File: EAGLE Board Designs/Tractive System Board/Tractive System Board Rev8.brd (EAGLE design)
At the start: 200 x 65 mm, 143 parts, among them J1 CONNECTOR-5_MICRO_V7S_, J2 CONNECTOR-5_MICRO_V6S_, J3 CONNECTOR-8_μF_T_V_BLACK, K1 RELAY_SPST_NO_D_24, Q2 TRANSISTOR_N_MOS__PMV15ENEA, U10 LTC6994-2, U5 RELAY_SOLIDSTATE_NO_AB38S-Q-A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, U6 LT8315, U7 AMC3330_AIRGAP, U8 AMC3330_AIRGAP

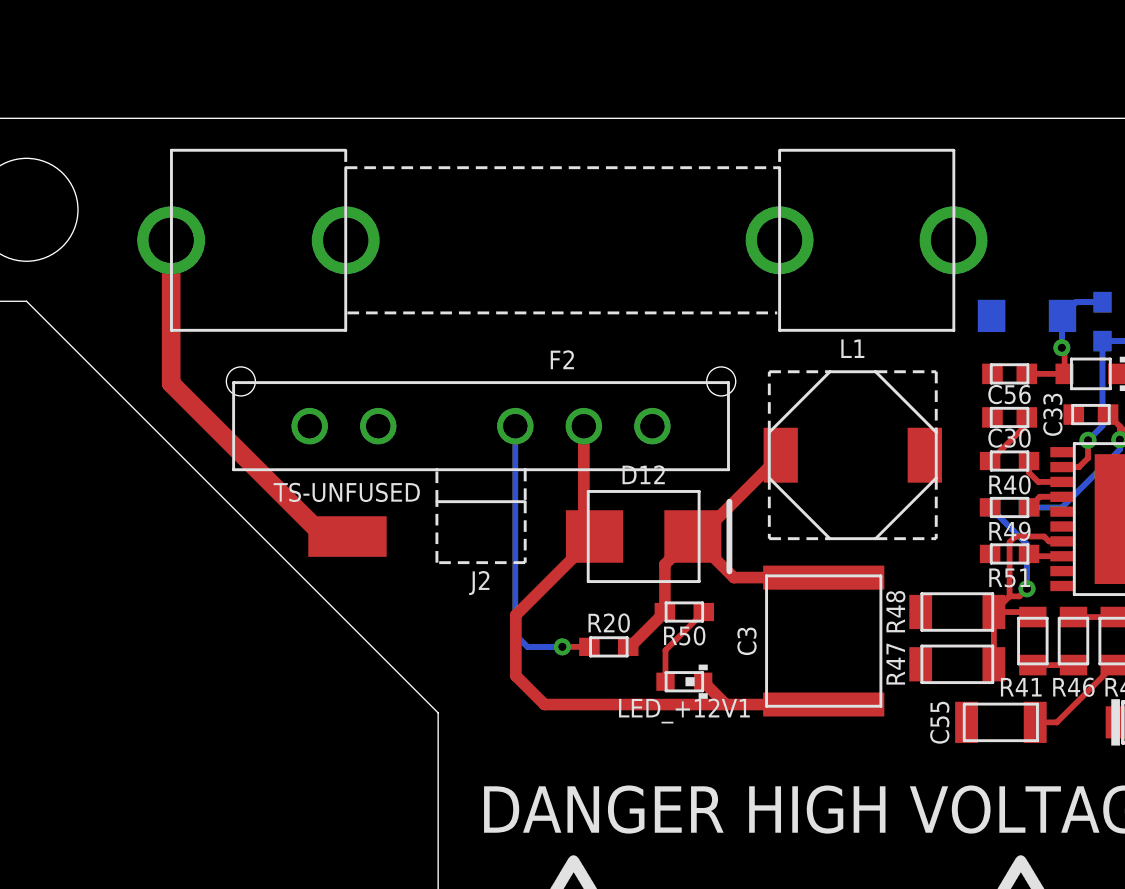
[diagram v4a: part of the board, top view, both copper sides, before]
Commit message: tsb-rev8-layout-update
space between connector and fuse on TS- side
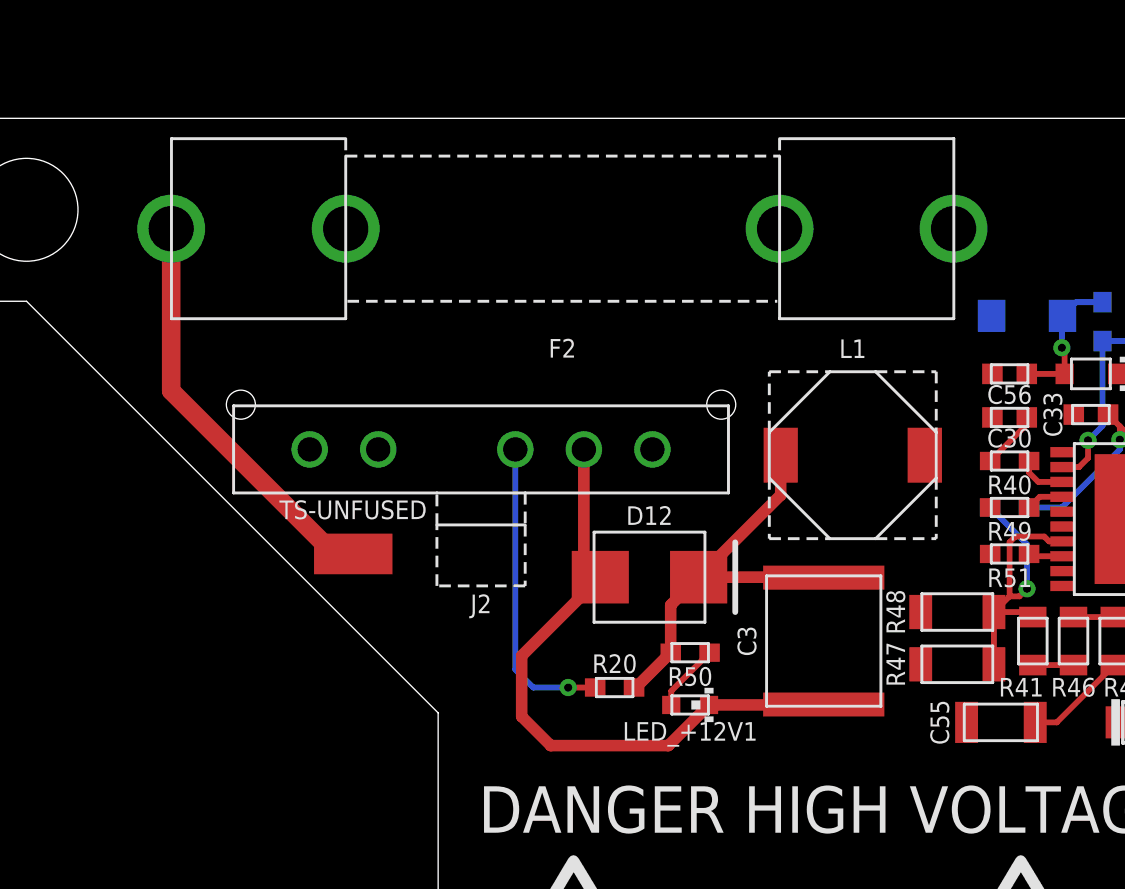
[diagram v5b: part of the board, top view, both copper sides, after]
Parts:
- moved R50 1.80 mm to (33.0, -23.4)
- moved D12 1.80 mm to (31.2, -20.1)
- moved R20 1.80 mm to (29.7, -24.9)
- moved LED_+12V1 1.05 mm to (33.0, -25.7)
- moved J2 1.02 mm to (23.9, -14.5)
- moved TS-UNFUSED 0.80 mm to (18.3, -19.1)
- moved F2 0.51 mm to (27.4, -4.83)
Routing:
- net TS-UNFUSED: track 34.4 -> 36.6 mm
- net TS-FUSED: track 91.0 -> 91.9 mm
- net AIL+: track 12.6 -> 13.4 mm
- net TS+12V: track 18.7 -> 19.5 mm
- net N$44: track 3.74 -> 2.98 mm

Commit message: tsb-rev8-layout-update
Made buck convert PGND connections to internal plane
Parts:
- moved D9 1.55 mm to (49.3, -8.89), flipped to the top, turned to 0 degrees
- moved R30 0.25 mm to (96.5, -47.0)
- moved R42 0.25 mm to (95.0, -47.0)
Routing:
- net PGND: track 1.31 -> 24.4 mm, vias 1 -> 11
- net TS+12V: track 19.5 -> 32.7 mm
- net IT+: track 95.8 -> 90.0 mm
- net DCDC_ENABLE: track 75.1 -> 70.7 mm
- net N$55: track 6.26 -> 7.71 mm
- net PRECHARGE_OK: track 82.3 -> 82.9 mm
- net GND: track 97.8 -> 98.5 mm

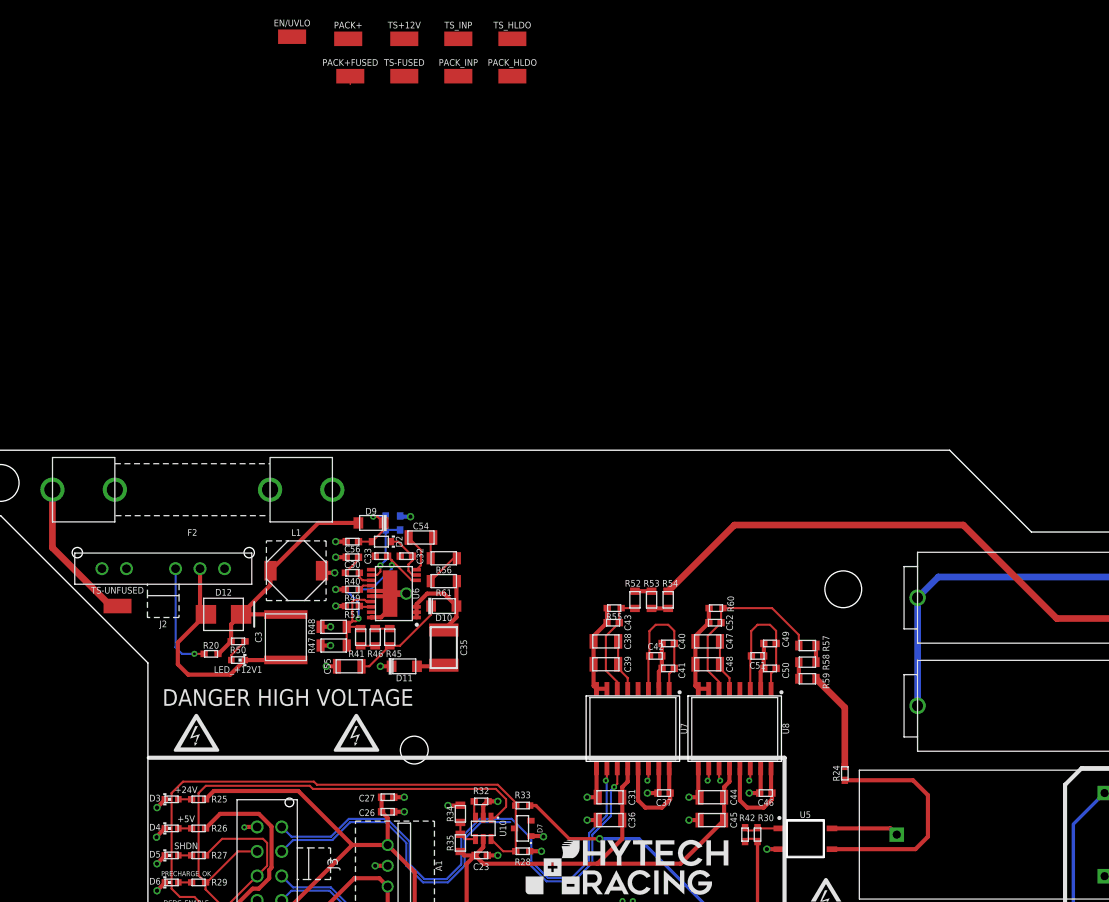
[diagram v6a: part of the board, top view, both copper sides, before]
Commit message: tsb-rev8-layout-update
Finished buck converter routing. Routed TS-FUSED to iso amps and buck. Placed TPs. Readjusted all via drill sizes to match hv pcb width
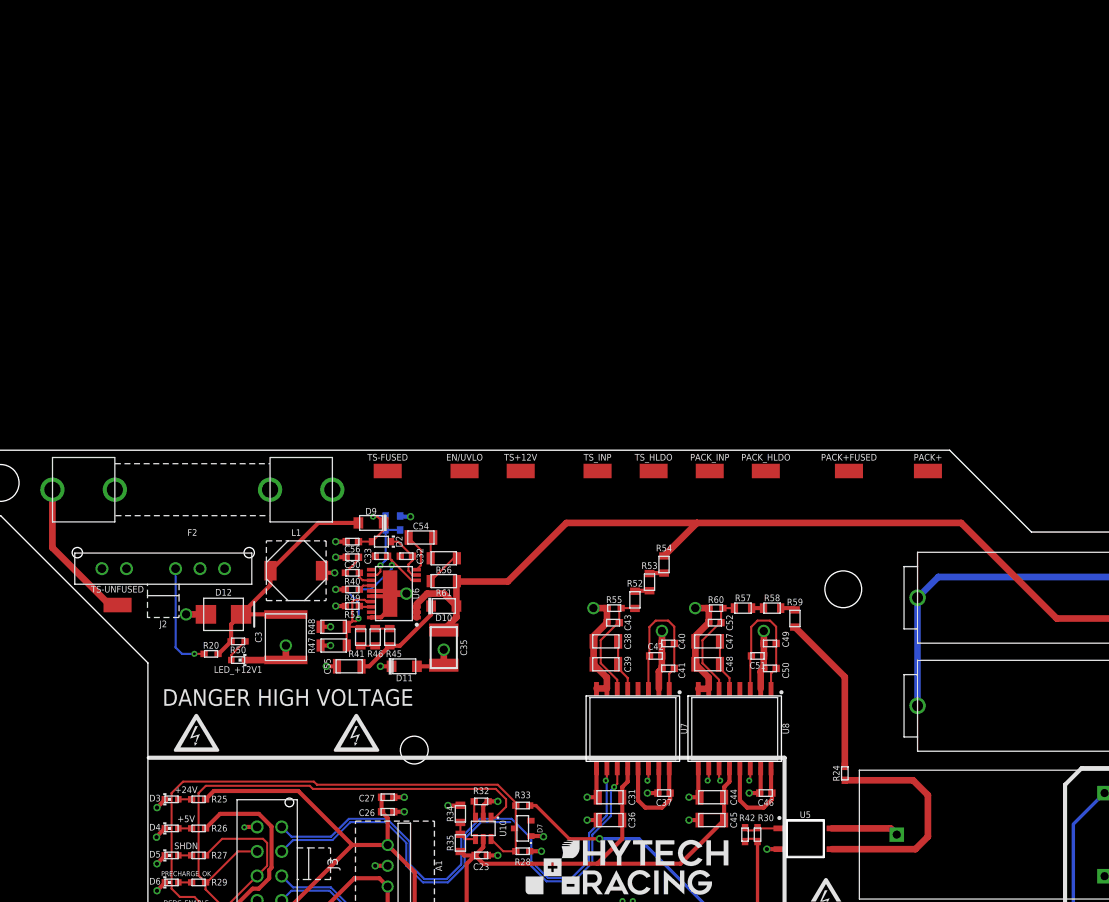
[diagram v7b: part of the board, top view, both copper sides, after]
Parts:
- moved PACK+ 88.4 mm to (117.3, -2.54)
- moved PACK+FUSED 77.8 mm to (107.7, -2.54)
- moved PACK_HLDO 57.4 mm to (97.5, -2.54)
- moved PACK_INP 57.2 mm to (90.7, -2.54)
- moved EN/UVLO 57.1 mm to (60.7, -2.54)
- moved TS_HLDO 55.6 mm to (83.8, -2.54)
- moved TS_INP 55.5 mm to (77.0, -2.54)
- moved TS+12V 54.7 mm to (67.6, -2.54)
- moved TS-FUSED 48.3 mm to (51.3, -2.54)
- moved R57 9.11 mm to (94.7, -19.3)
- moved R58 7.89 mm to (98.3, -19.3), turned to 0 degrees
- moved R59 7.52 mm to (101.1, -20.6), turned to 270 degrees
- moved R54 4.35 mm to (85.1, -14.0)
- moved R53 2.17 mm to (83.3, -16.1), turned to 90 degrees
- moved TS-UNFUSED 0.13 mm to (18.3, -18.9)
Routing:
- net TS-FUSED: track 92.0 -> 167.4 mm, vias 0 -> 7
- net TS+FUSED: track 148.5 -> 179.8 mm
- net PACK_INP: track 23.4 -> 13.4 mm
- net PACK+FUSED: track 13.2 -> 19.5 mm
- net N$64: track 18.1 -> 19.1 mm
- net N$51: track 18.1 -> 19.1 mm
- net TS_INP: track 13.4 -> 14.0 mm
- net N$65: track 2.03 -> 1.46 mm

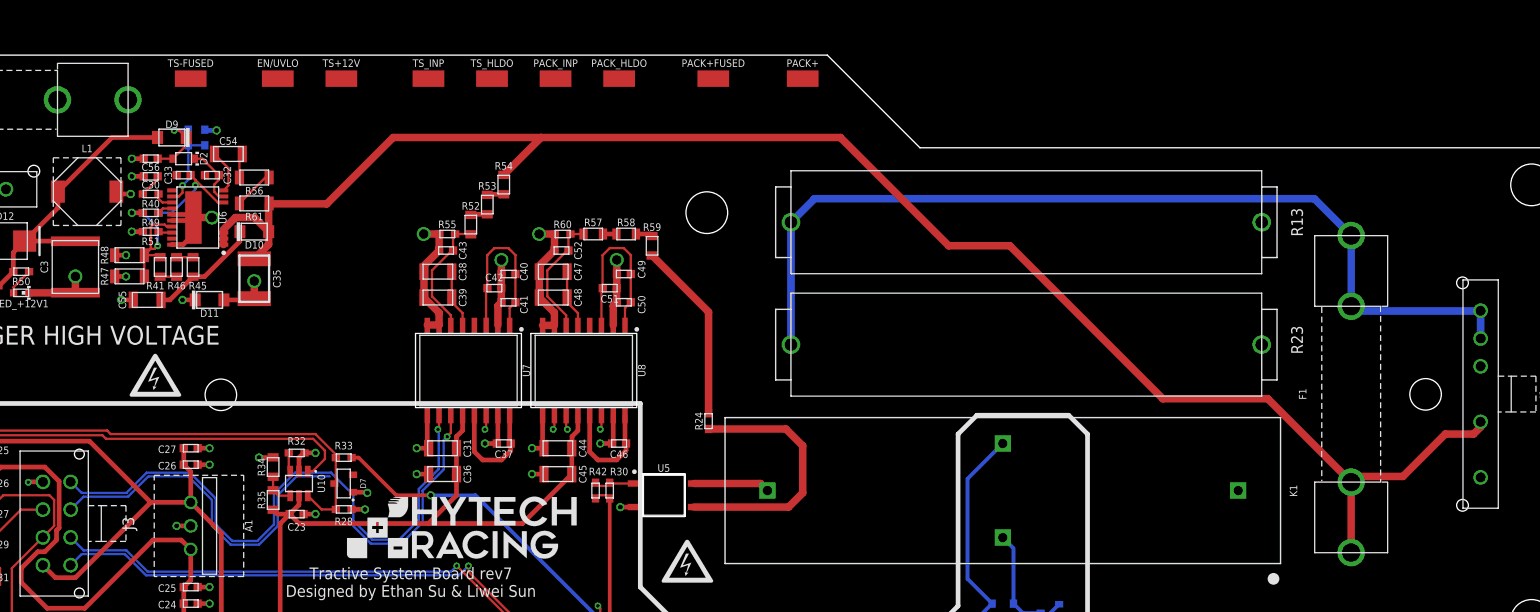
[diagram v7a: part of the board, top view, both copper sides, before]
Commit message: tsb-rev8-layout-update
tp routing and more consolidated HV spacing
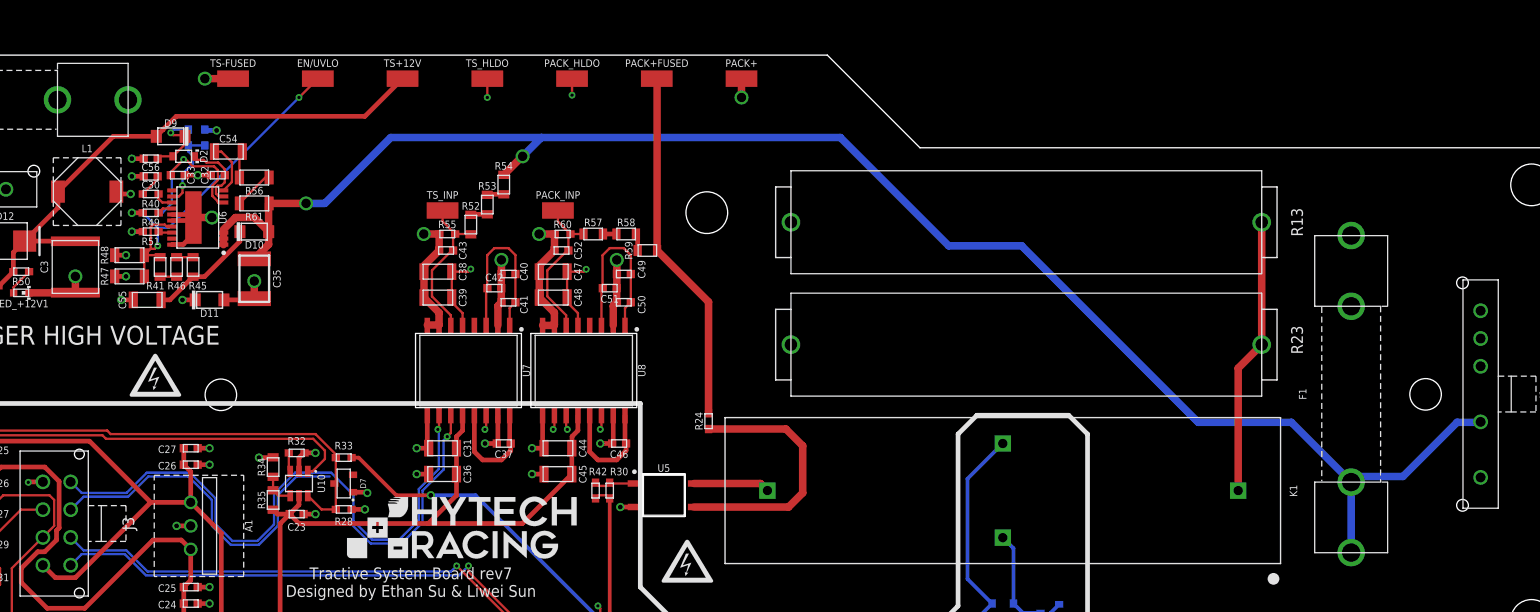
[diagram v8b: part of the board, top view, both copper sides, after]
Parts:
- moved TS_INP 14.3 mm to (78.5, -16.8)
- moved PACK_INP 14.2 mm to (90.9, -16.8)
- moved TS+12V 6.60 mm to (74.2, -2.54)
- moved PACK+ 6.60 mm to (110.7, -2.54)
- moved PACK+FUSED 6.10 mm to (101.6, -2.54)
- moved PACK_HLDO 5.08 mm to (92.5, -2.54)
- moved TS-FUSED 4.57 mm to (55.9, -2.54)
- moved EN/UVLO 4.32 mm to (65.0, -2.54)
- moved R59 0.72 mm to (100.6, -21.1), turned to 0 degrees
- moved C32 0.63 mm to (54.2, -13.0)
- moved C33 0.63 mm to (49.9, -13.0), turned to 0 degrees
- moved TS_HLDO 0.51 mm to (83.3, -2.54)
- moved C54 0.25 mm to (55.4, -10.4)
- moved D2 0.25 mm to (50.5, -10.9)
- moved D9 0.18 mm to (49.1, -8.76)
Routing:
- net PACK+: track 104.8 -> 147.6 mm, vias 0 -> 1
- net TS+12V: track 32.7 -> 61.8 mm
- net EN/UVLO: track 15.0 -> 39.0 mm, vias 1 -> 2
- net TS_HLDO_OUT: track 6.28 -> 29.7 mm, vias 0 -> 2
- net PACK_HLDO_OUT: track 6.28 -> 29.6 mm, vias 0 -> 2
- net PACK+FUSED: track 19.5 -> 38.4 mm
- net TS-FUSED: track 167.4 -> 179.7 mm, vias 7 -> 8
- net INTVCC: track 10.8 -> 18.2 mm
- net PACK_INP: track 13.4 -> 16.5 mm
- net TS_INP: track 14.0 -> 17.1 mm
- net PGND: track 24.4 -> 27.3 mm, vias 11 -> 12
- net N$49: track 6.59 -> 8.27 mm
- net N$38: track 4.77 -> 5.80 mm
- net FB: track 8.45 -> 9.05 mm
- net N$55: track 7.71 -> 8.21 mm
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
